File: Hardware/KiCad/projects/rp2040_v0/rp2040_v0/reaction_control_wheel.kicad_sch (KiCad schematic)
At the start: 13 parts, among them J16 Conn_01x03, J22 Conn_02x05_Odd_Even, J23 Screw_Terminal_01x02, U12 DRV8837

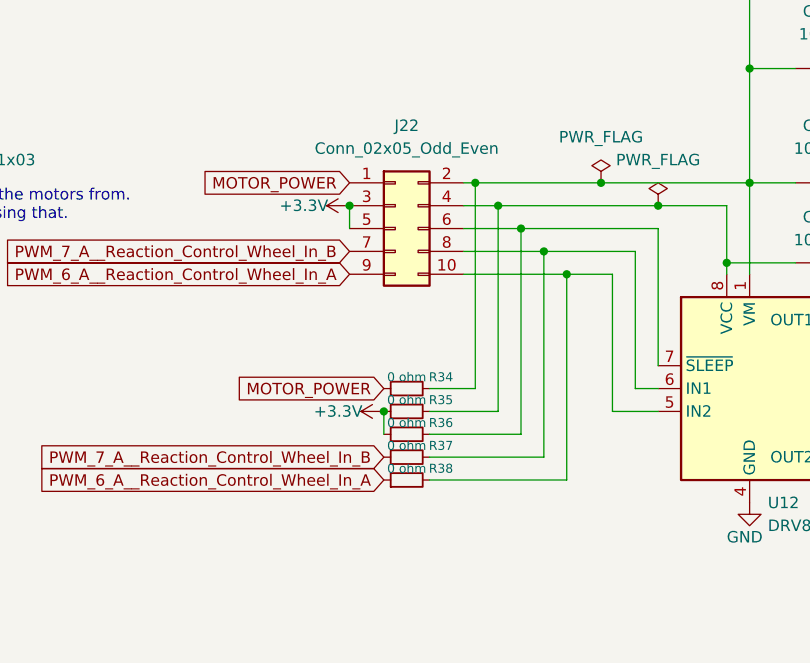
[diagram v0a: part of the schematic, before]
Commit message: Moved reaction control wheel pin numbers around for easier routing.
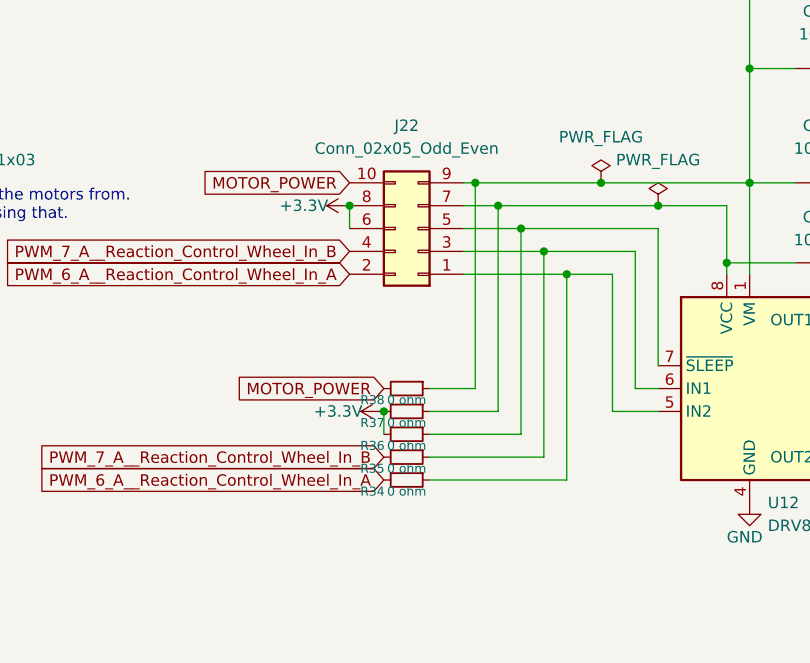
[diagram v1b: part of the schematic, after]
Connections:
- net +3.3V: now also J22.6 (Pin_6), J22.8 (Pin_8), R36.2, R37.2; no longer J22.3 (Pin_3), J22.5 (Pin_5), R35.1, R36.1
- net MOTOR_POWER: now also J22.10 (Pin_10), R38.2; no longer J22.1 (Pin_1), R34.1
- net PWM_6_A__Reaction_Control_Wheel_In_A: now also J22.2 (Pin_2), R34.2; no longer J22.9 (Pin_9), R38.1
- net PWM_7_A__Reaction_Control_Wheel_In_B: now also J22.4 (Pin_4), R35.2; no longer J22.7 (Pin_7), R37.1
- net at C37.1, C38.1, C39.1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: now also J22.9 (Pin_9), R38.1; no longer J22.2 (Pin_2), R34.2
- net at C40.1, U12.8 (VCC): now also J22.7 (Pin_7), R37.1; no longer J22.4 (Pin_4), R35.2
- new net: J22.1 (Pin_1), R34.1, U12.5 (IN2)
- new net: J22.3 (Pin_3), R35.1, U12.6 (IN1)
- new net: J22.5 (Pin_5), R36.1, U12.7 (~{SLEEP})
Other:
- moved on the sheet: J22, R34, R35, R36, R37, R38
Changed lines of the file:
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@@
   (junction (at 139.7 86.36) (diameter 0) (color 0 0 0 0)
   )
+  (junction (at 185.42 95.25) (diameter 0) (color 0 0 0 0)
+  )
+  (junction (at 147.32 93.98) (diameter 0) (color 0 0 0 0)
+  )
+  (junction (at 142.24 88.9) (diameter 0) (color 0 0 0 0)
+  )
+  (junction (at 129.54 111.76) (diameter 0) (color 0 0 0 0)
+  )
+  (junction (at 170.18 86.36) (diameter 0) (color 0 0 0 0)
+  )
   (junction (at 125.73 88.9) (diameter 0) (color 0 0 0 0)
-  )
-  (junction (at 129.54 111.76) (diameter 0) (color 0 0 0 0)
-  )
-  (junction (at 185.42 95.25) (diameter 0) (color 0 0 0 0)
-  )
-  (junction (at 147.32 93.98) (diameter 0) (color 0 0 0 0)
-  )
-  (junction (at 142.24 88.9) (diameter 0) (color 0 0 0 0)
-  )
-  (junction (at 170.18 86.36) (diameter 0) (color 0 0 0 0)
   )
   (junction (at 167.64 95.25) (diameter 0) (color 0 0 0 0)
@@
     )
   )
-  (symbol (lib_id "Device:R_Small") (at 132.08 109.22 90) (unit 1)
-    (in_bom yes) (on_board yes)
-    (property "Reference" "R34" (id 0) (at 135.89 107.95 90)
-      (effects (font (size 1 1)))
-    )
-    (property "Value" "0 ohm" (id 1) (at 132.08 107.95 90)
-      (effects (font (size 1 1)))
-    )
-    (property "Footprint" "Resistor_SMD:R_0402_1005Metric" (id 2) (at 132.08 109.22 0)
-      (effects (font (size 1.27 1.27)) hide)
-    )
-    (property "Datasheet" "~" (id 3) (at 132.08 109.22 0)
-      (effects (font (size 1.27 1.27)) hide)
-    )
-    (pin "1")
-    (pin "2")
-  )
-  (symbol (lib_id "Connector_Generic:Conn_02x05_Odd_Even") (at 130.81 91.44 0) (unit 1)
+  (symbol (lib_id "Device:R_Small") (at 132.08 119.38 270) (unit 1)
+    (in_bom yes) (on_board yes)
+    (property "Reference" "R34" (id 0) (at 128.27 120.65 90)
+      (effects (font (size 1 1)))
+    )
+    (property "Value" "0 ohm" (id 1) (at 132.08 120.65 90)
+      (effects (font (size 1 1)))
+    )
+    (property "Footprint" "Resistor_SMD:R_0402_1005Metric" (id 2) (at 132.08 119.38 0)
+      (effects (font (size 1.27 1.27)) hide)
+    )
+    (property "Datasheet" "~" (id 3) (at 132.08 119.38 0)
+      (effects (font (size 1.27 1.27)) hide)
+    )
+    (pin "1")
+    (pin "2")
+  )
+  (symbol (lib_id "Connector_Generic:Conn_02x05_Odd_Even") (at 133.35 91.44 180) (unit 1)
     (in_bom yes) (on_board yes) (fields_autoplaced)
     (property "Reference" "J22" (id 0) (at 132.08 80.01 0))
     (property "Value" "Conn_02x05_Odd_Even" (id 1) (at 132.08 82.55 0))
-    (property "Footprint" "Connector_PinHeader_2.54mm:PinHeader_2x05_P2.54mm_Vertical" (id 2) (at 130.81 91.44 0)
-      (effects (font (size 1.27 1.27)) hide)
-    )
-    (property "Datasheet" "~" (id 3) (at 130.81 91.44 0)
+    (property "Footprint" "Connector_PinHeader_2.54mm:PinHeader_2x05_P2.54mm_Vertical" (id 2) (at 133.35 91.44 0)
+      (effects (font (size 1.27 1.27)) hide)
+    )
+    (property "Datasheet" "~" (id 3) (at 133.35 91.44 0)
       (effects (font (size 1.27 1.27)) hide)
     )
@@
     (pin "3")
   )
-  (symbol (lib_id "Device:R_Small") (at 132.08 116.84 90) (unit 1)
-    (in_bom yes) (on_board yes)
-    (property "Reference" "R37" (id 0) (at 135.89 115.57 90)
-      (effects (font (size 1 1)))
-    )
-    (property "Value" "0 ohm" (id 1) (at 132.08 115.57 90)
-      (effects (font (size 1 1)))
-    )
-    (property "Footprint" "Resistor_SMD:R_0402_1005Metric" (id 2) (at 132.08 116.84 0)
-      (effects (font (size 1.27 1.27)) hide)
-    )
-    (property "Datasheet" "~" (id 3) (at 132.08 116.84 0)
+  (symbol (lib_id "Device:R_Small") (at 132.08 111.76 270) (unit 1)
+    (in_bom yes) (on_board yes)
+    (property "Reference" "R37" (id 0) (at 128.27 113.03 90)
+      (effects (font (size 1 1)))
+    )
+    (property "Value" "0 ohm" (id 1) (at 132.08 113.03 90)
+      (effects (font (size 1 1)))
+    )
+    (property "Footprint" "Resistor_SMD:R_0402_1005Metric" (id 2) (at 132.08 111.76 0)
+      (effects (font (size 1.27 1.27)) hide)
+    )
+    (property "Datasheet" "~" (id 3) (at 132.08 111.76 0)
       (effects (font (size 1.27 1.27)) hide)
     )
@@
     (pin "1")
   )
-  (symbol (lib_id "Device:R_Small") (at 132.08 114.3 90) (unit 1)
-    (in_bom yes) (on_board yes)
-    (property "Reference" "R36" (id 0) (at 135.89 113.03 90)
-      (effects (font (size 1 1)))
-    )
-    (property "Value" "0 ohm" (id 1) (at 132.08 113.03 90)
+  (symbol (lib_id "Device:R_Small") (at 132.08 114.3 270) (unit 1)
+    (in_bom yes) (on_board yes)
+    (property "Reference" "R36" (id 0) (at 128.27 115.57 90)
+      (effects (font (size 1 1)))
+    )
+    (property "Value" "0 ohm" (id 1) (at 132.08 115.57 90)
       (effects (font (size 1 1)))
     )
@@
     (pin "1")
   )
-  (symbol (lib_id "Device:R_Small") (at 132.08 111.76 90) (unit 1)
-    (in_bom yes) (on_board yes)
-    (property "Reference" "R35" (id 0) (at 135.89 110.49 90)
-      (effects (font (size 1 1)))
-    )
-    (property "Value" "0 ohm" (id 1) (at 132.08 110.49 90)
-      (effects (font (size 1 1)))
-    )
-    (property "Footprint" "Resistor_SMD:R_0402_1005Metric" (id 2) (at 132.08 111.76 0)
-      (effects (font (size 1.27 1.27)) hide)
-    )
-    (property "Datasheet" "~" (id 3) (at 132.08 111.76 0)
+  (symbol (lib_id "Device:R_Small") (at 132.08 116.84 270) (unit 1)
+    (in_bom yes) (on_board yes)
+    (property "Reference" "R35" (id 0) (at 128.27 118.11 90)
+      (effects (font (size 1 1)))
+    )
+    (property "Value" "0 ohm" (id 1) (at 132.08 118.11 90)
+      (effects (font (size 1 1)))
+    )
+    (property "Footprint" "Resistor_SMD:R_0402_1005Metric" (id 2) (at 132.08 116.84 0)
+      (effects (font (size 1.27 1.27)) hide)
+    )
+    (property "Datasheet" "~" (id 3) (at 132.08 116.84 0)
       (effects (font (size 1.27 1.27)) hide)
     )
@@
     (pin "2")
   )
-  (symbol (lib_id "Device:R_Small") (at 132.08 119.38 90) (unit 1)
-    (in_bom yes) (on_board yes)
-    (property "Reference" "R38" (id 0) (at 135.89 118.11 90)
-      (effects (font (size 1 1)))
-    )
-    (property "Value" "0 ohm" (id 1) (at 132.08 118.11 90)
-      (effects (font (size 1 1)))
-    )
-    (property "Footprint" "Resistor_SMD:R_0402_1005Metric" (id 2) (at 132.08 119.38 0)
-      (effects (font (size 1.27 1.27)) hide)
-    )
-    (property "Datasheet" "~" (id 3) (at 132.08 119.38 0)
-      (effects (font (size 1.27 1.27)) hide)
-    )
+  (symbol (lib_id "Device:R_Small") (at 132.08 109.22 270) (unit 1)
+    (in_bom yes) (on_board yes)
+    (property "Reference" "R38" (id 0) (at 128.27 110.49 90)
+      (effects (font (size 1 1)))
+    )
+    (property "Value" "0 ohm" (id 1) (at 132.08 110.49 90)
+      (effects (font (size 1 1)))
+    )
+    (property "Footprint" "Resistor_SMD:R_0402_1005Metric" (id 2) (at 132.08 109.22 0)
+      (effects (font (size 1.27 1.27)) hide)
+    )
+    (property "Datasheet" "~" (id 3) (at 132.08 109.22 0)
+      (effects (font (size 1.27 1.27)) hide)
+    )
